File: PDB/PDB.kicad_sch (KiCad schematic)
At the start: 45 parts, among them J1 Conn_01x02, J2 Conn_01x04, Q1 S8050, Sw1 D-SWITCH_MR5-111-C5N-BB

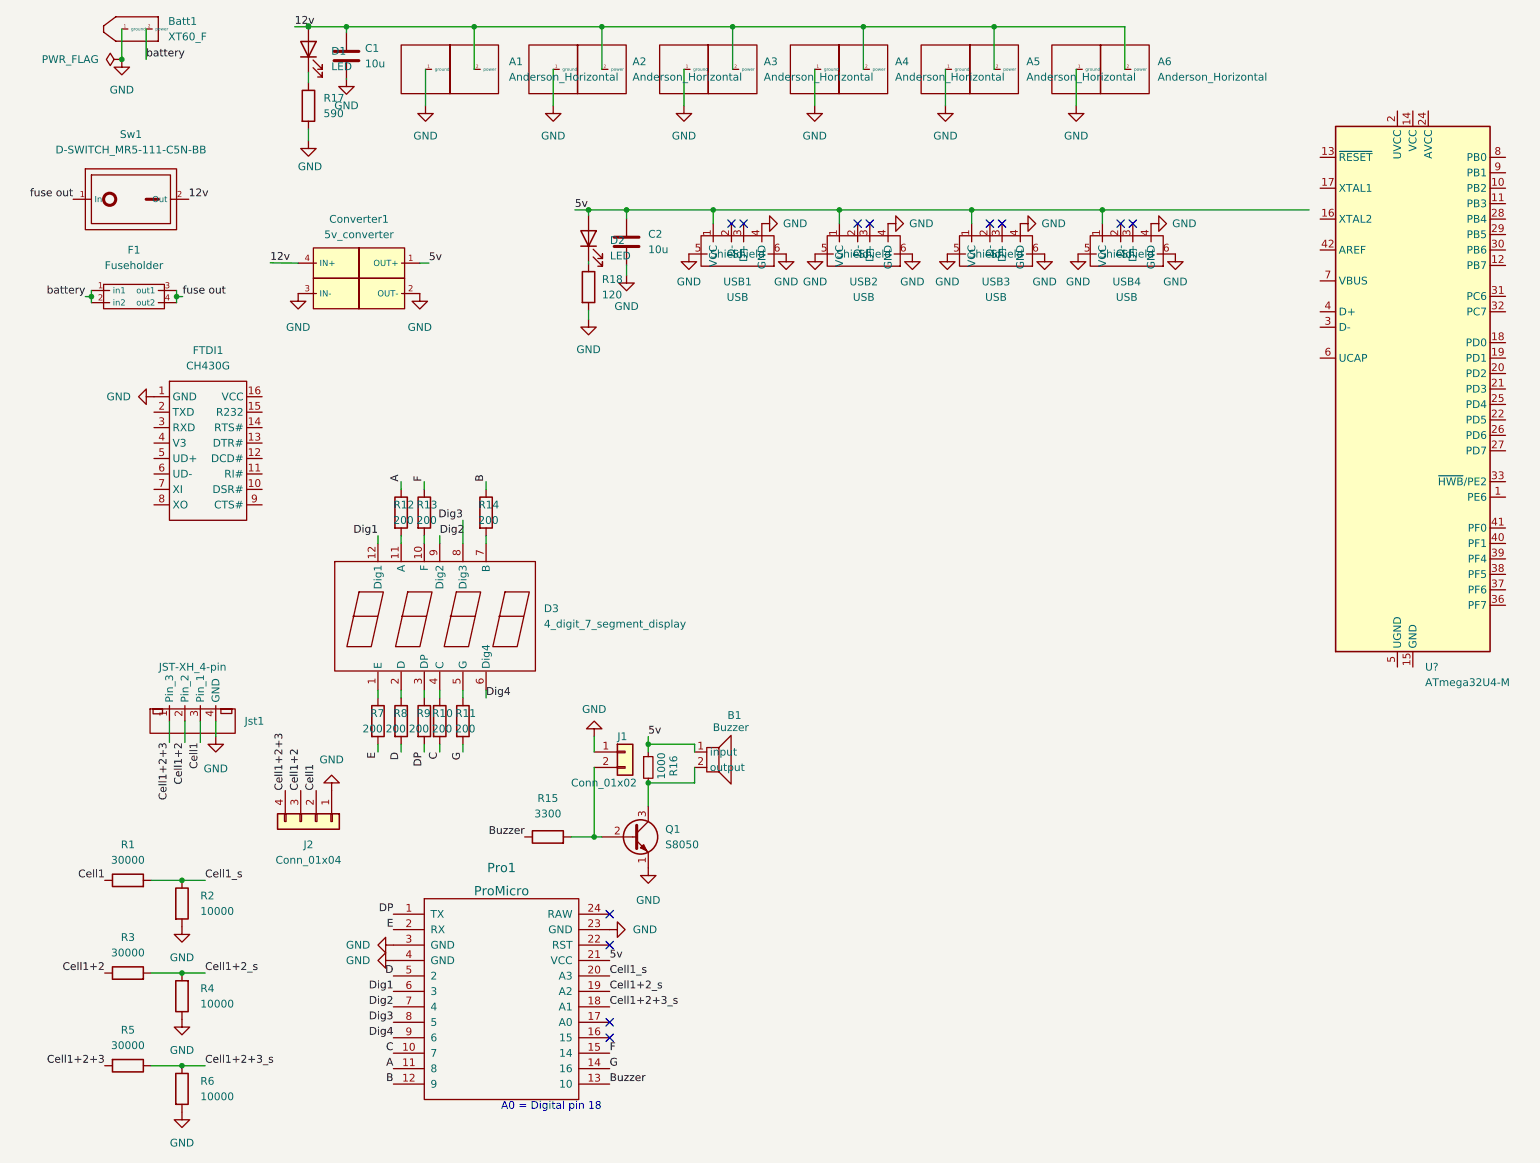
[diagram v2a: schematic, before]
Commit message: revised layout for smaller size
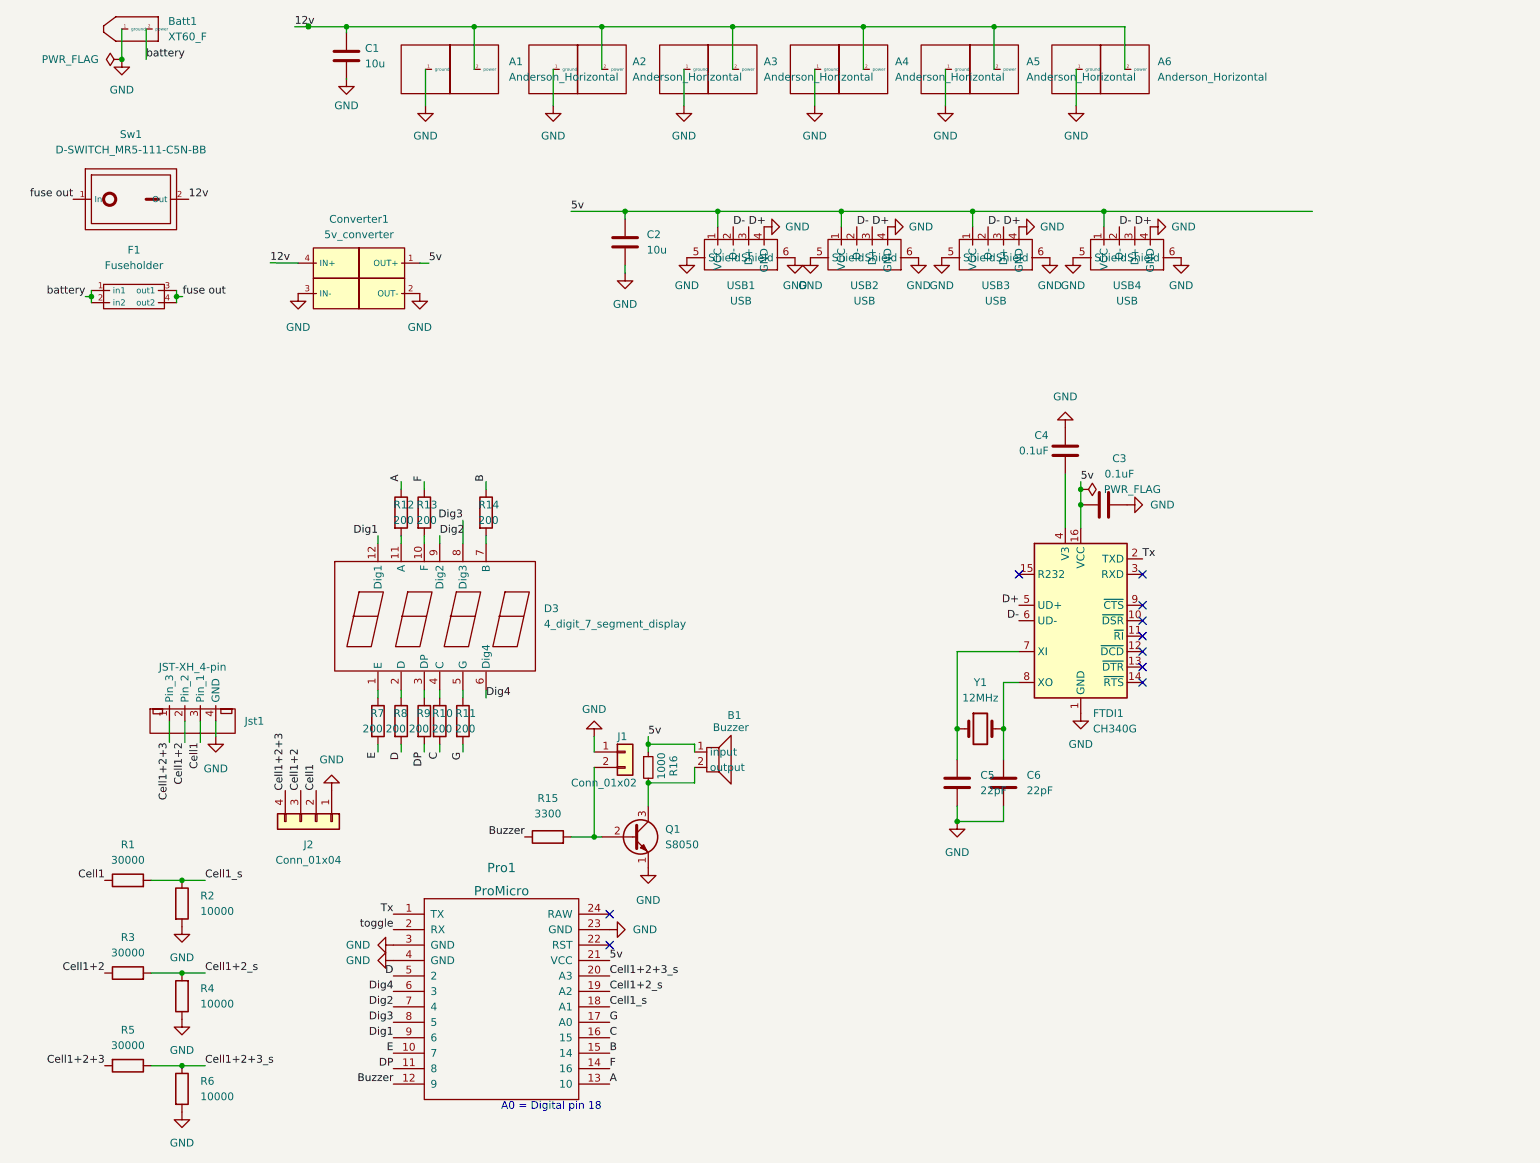
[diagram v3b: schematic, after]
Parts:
- removed D1, D2: LED, LED_SMD:LED_0603_1608Metric, symbol Device:LED
- removed FTDI1: CH430G, symbol PiE_Symbols:CH430G
- removed R17: 590, Resistor_SMD:R_1210_3225Metric, symbol Device:R
- removed R18: 120, Resistor_SMD:R_0603_1608Metric, symbol Device:R
- removed U?: ATmega32U4-M, Package_DFN_QFN:QFN-44-1EP_7x7mm_P0.5mm_EP5.2x5.2mm, symbol MCU_Microchip_ATmega:ATmega32U4-M
- added C3, C4: 0.1uF, Capacitor_SMD:C_0603_1608Metric, symbol Device:C
- added C5, C6: 22pF, Capacitor_SMD:C_0603_1608Metric, symbol Device:C
- added FTDI1: CH340G, Package_SO:SOIC-16_3.9x9.9mm_P1.27mm, symbol Interface_USB:CH340G
- added Y1: 12MHz, Crystal:Crystal_HC49-U_Vertical, symbol Device:Crystal
- C1, C2: footprint Capacitor_SMD:C_0805_2012Metric -> Capacitor_THT:CP_Radial_D5.0mm_P2.00mm
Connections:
- net 5v: now also C3.1, FTDI1.16 (VCC)
- net A: now also Pro1.13 (10); no longer Pro1.11 (8)
- net B: now also Pro1.15 (14); no longer Pro1.12 (9)
- net Buzzer: now also Pro1.12 (9); no longer Pro1.13 (10)
- net C: now also Pro1.16 (15); no longer Pro1.10 (7)
- net Cell1+2+3_s: now also Pro1.20 (A3); no longer Pro1.18 (A1)
- net Cell1_s: now also Pro1.18 (A1); no longer Pro1.20 (A3)
- net DP: now also Pro1.11 (8); no longer Pro1.1 (TX)
- net Dig1: now also Pro1.9 (6); no longer Pro1.6 (3)
- net Dig4: now also Pro1.6 (3); no longer Pro1.9 (6)
- net E: now also Pro1.10 (7); no longer Pro1.2 (RX)
- net F: now also Pro1.14 (16); no longer Pro1.15 (14)
- net G: now also Pro1.17 (A0); no longer Pro1.14 (16)
- net GND: now also C3.2, C4.2, C5.2, C6.2, FTDI1.1 (GND)
- net D-: now reaches USB3.2 (D-)
- net D-: now also USB1.2 (D-), USB2.2 (D-), USB4.2 (D-), FTDI1.6 (UD-)
- net D+: now reaches USB3.3 (D+)
- net D+: now also USB1.3 (D+), USB2.3 (D+), USB4.3 (D+), FTDI1.5 (UD+)
- new net: C5.1, FTDI1.7 (XI), Y1.1
- new net: C6.1, FTDI1.8 (XO), Y1.2
- new net: C4.1, FTDI1.4 (V3)
- new net Tx: FTDI1.2 (TXD), Pro1.1 (TX)
- new net toggle: Pro1.2 (RX)
- no-connect marks 12 -> 10
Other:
- moved on the sheet: USB1, USB2, USB3, USB4

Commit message: Finished board layout?
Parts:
- added C7: 0.1u, Capacitor_SMD:C_0603_1608Metric, symbol Device:C
- added R17, R18: 22, Resistor_SMD:R_0603_1608Metric, symbol Device:R
- added SW2: SW_SPDT, PiE_Footprints:DEALON SS-12D01-G3, symbol Switch:SW_SPDT
- added U3: PCF8574, PiE_Footprints:PCF8574T, symbol Interface_Expansion:PCF8574
- Batt1: footprint PiE_Footprints:XT60_F -> PiE_Footprints:AMASS_XT60-M_1x02_P7.20mm_Vertical
- J1: footprint Connector_PinHeader_2.54mm:PinHeader_1x02_P2.54mm_Vertical -> PiE_Footprints:PinHeader_1x02_P2.54mm_Vertical
- J2: footprint Connector_PinHeader_2.54mm:PinHeader_1x04_P2.54mm_Vertical -> PiE_Footprints:PinHeader_1x04_P2.54mm_Vertical
- Jst1: footprint PiE_Footprints:JST_XH_B4B-XH-AM_1x04_P2.50mm_Vertical -> PiE_Footprints:JST_XH_B4B-XH-A_1x04_P2.50mm_Vertical
- Y1: footprint Crystal:Crystal_HC49-U_Vertical -> PiE_Footprints:JYJE S1C12000VWFAC
- renumbered USB4 to DATA1, FTDI1 to U2
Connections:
- net 5v: now also C7.2, SW2.1 (A), U3.16 (VDD)
- net A: now also U3.7 (P3); no longer Pro1.13 (10)
- net B: now also U3.9 (P4); no longer Pro1.15 (14)
- net Buzzer: now also Pro1.13 (10); no longer Pro1.12 (9)
- net C: now also U3.11 (P6); no longer Pro1.16 (15)
- net Cell1+2+3_s: now also Pro1.18 (A1); no longer Pro1.20 (A3)
- net Cell1_s: now also Pro1.20 (A3); no longer Pro1.18 (A1)
- net D: now also U3.5 (P1); no longer Pro1.5 (2)
- net D+: now also R18.1; no longer DATA1.3 (D+), USB1.3 (D+), USB2.3 (D+), USB3.3 (D+)
- net D-: now also R17.1; no longer DATA1.2 (D-), USB1.2 (D-), USB2.2 (D-), USB3.2 (D-)
- net DP: now also U3.6 (P2); no longer Pro1.11 (8)
- net Dig1: now also Pro1.17 (A0); no longer Pro1.9 (6)
- net Dig2: now also Pro1.16 (15); no longer Pro1.7 (4)
- net Dig3: now also Pro1.15 (14); no longer Pro1.8 (5)
- net Dig4: now also Pro1.12 (9); no longer Pro1.6 (3)
- net E: now also U3.4 (P0); no longer Pro1.10 (7)
- net F: now also U3.10 (P5); no longer Pro1.14 (16)
- net G: now also U3.12 (P7); no longer Pro1.17 (A0)
- net GND: now also C7.1, SW2.3 (C), U3.1 (A0), U3.2 (A1), U3.3 (A2), U3.8 (VSS)
- net toggle: now also Pro1.14 (16), SW2.2 (B); no longer Pro1.2 (RX)
- net Rx: now reaches U2.3 (RXD)
- net Rx: now also Pro1.2 (RX)
- new net: DATA1.3 (D+), R18.2
- new net: DATA1.2 (D-), R17.2
- new net SCL: Pro1.6 (3), U3.14 (SCL)
- new net SDA: Pro1.5 (2), U3.15 (SDA)
- no-connect marks 10 -> 16
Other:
- moved on the sheet: B1, C2, C3, C4, C5, C6, Converter1, D3, DATA1, J1, J2, Q1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

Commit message: ordered this ****
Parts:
- added R19, R20: 4700, Resistor_SMD:R_0603_1608Metric, symbol Device:R
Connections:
- net 5v: now also R19.1, R20.1
- net SCL: now also R19.2
- net SDA: now also R20.2
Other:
- moved on the sheet: C7
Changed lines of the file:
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@@
   (junction (at 38 61) (diameter 0) (color 0 0 0 0)
   )
+  (junction (at 205.74 101.6) (diameter 0) (color 0 0 0 0)
+  )
   (junction (at 238.76 46.99) (diameter 0) (color 0 0 0 0)
   )
   (junction (at 38.89 157) (diameter 0) (color 0 0 0 0)
   )
+  (junction (at 220.98 88.9) (diameter 0) (color 0 0 0 0)
+  )
   (junction (at 125.73 40.64) (diameter 0) (color 0 0 0 0)
   )
@@
   (junction (at 92.71 97.79) (diameter 0) (color 0 0 0 0)
   )
-  (junction (at 220.98 88.9) (diameter 0) (color 0 0 0 0)
-  )
   (junction (at 92.71 100.33) (diameter 0) (color 0 0 0 0)
   )
   (junction (at 59.69 16.63) (diameter 0) (color 0 0 0 0)
   )
+  (junction (at 205.74 88.9) (diameter 0) (color 0 0 0 0)
+  )
   (junction (at 38.89 187.48) (diameter 0) (color 0 0 0 0)
+  )
+  (junction (at 201.93 99.06) (diameter 0) (color 0 0 0 0)
   )
   (junction (at 29 22) (diameter 0) (color 0 0 0 0)
@@
     (stroke (width 0) (type default) (color 0 0 0 0))
   )
+  (wire (pts (xy 200.66 101.6) (xy 205.74 101.6))
+    (stroke (width 0) (type default) (color 0 0 0 0))
+  )
   (wire (pts (xy 39.37 130.81) (xy 39.37 134.31))
     (stroke (width 0) (type default) (color 0 0 0 0))
@@
     (stroke (width 0) (type default) (color 0 0 0 0))
   )
+  (wire (pts (xy 205.74 88.9) (xy 220.98 88.9))
+    (stroke (width 0) (type default) (color 0 0 0 0))
+  )
   (wire (pts (xy 38 61) (xy 38 62))
     (stroke (width 0) (type default) (color 0 0 0 0))
@@
     (stroke (width 0) (type default) (color 0 0 0 0))
   )
+  (wire (pts (xy 220.98 88.9) (xy 220.98 91.44))
+    (stroke (width 0) (type default) (color 0 0 0 0))
+  )
   (wire (pts (xy 72.39 124.46) (xy 72.39 132.08))
     (stroke (width 0) (type default) (color 0 0 0 0))
@@
     (stroke (width 0) (type default) (color 0 0 0 0))
   )
+  (wire (pts (xy 201.93 99.06) (xy 208.28 99.06))
+    (stroke (width 0) (type default) (color 0 0 0 0))
+  )
   (wire (pts (xy 44.45 130.81) (xy 44.45 133.35))
     (stroke (width 0) (type default) (color 0 0 0 0))
@@
     (stroke (width 0) (type default) (color 0 0 0 0))
   )
+  (wire (pts (xy 205.74 88.9) (xy 205.74 93.98))
+    (stroke (width 0) (type default) (color 0 0 0 0))
+  )
   (wire (pts (xy 129.44 16.63) (xy 129.44 23.63))
     (stroke (width 0) (type default) (color 0 0 0 0))
@@
     (stroke (width 0) (type default) (color 0 0 0 0))
   )
+  (wire (pts (xy 201.93 91.44) (xy 201.93 88.9))
+    (stroke (width 0) (type default) (color 0 0 0 0))
+  )
+  (wire (pts (xy 205.74 101.6) (xy 208.28 101.6))
+    (stroke (width 0) (type default) (color 0 0 0 0))
+  )
   (wire (pts (xy 172.44 16.63) (xy 172.44 23.63))
     (stroke (width 0) (type default) (color 0 0 0 0))
@@
     (stroke (width 0) (type default) (color 0 0 0 0))
   )
-  (wire (pts (xy 220.98 88.9) (xy 220.98 91.44))
-    (stroke (width 0) (type default) (color 0 0 0 0))
-  )
   (wire (pts (xy 90.17 40.64) (xy 90.17 41.91))
     (stroke (width 0) (type default) (color 0 0 0 0))
@@
     (stroke (width 0) (type default) (color 0 0 0 0))
   )
+  (wire (pts (xy 200.66 99.06) (xy 201.93 99.06))
+    (stroke (width 0) (type default) (color 0 0 0 0))
+  )
   (wire (pts (xy 208.28 111.76) (xy 205.74 111.76))
     (stroke (width 0) (type default) (color 0 0 0 0))
@@
     (stroke (width 0) (type default) (color 0 0 0 0))
   )
+  (wire (pts (xy 201.93 88.9) (xy 205.74 88.9))
+    (stroke (width 0) (type default) (color 0 0 0 0))
+  )
   (wire (pts (xy 24 60) (xy 24 61))
     (stroke (width 0) (type default) (color 0 0 0 0))
@@
     (stroke (width 0) (type default) (color 0 0 0 0))
   )
+  (wire (pts (xy 220.98 80.01) (xy 220.98 88.9))
+    (stroke (width 0) (type default) (color 0 0 0 0))
+  )
   (wire (pts (xy 172.44 16.63) (xy 193.94 16.63))
     (stroke (width 0) (type default) (color 0 0 0 0))
@@
     (stroke (width 0) (type default) (color 0 0 0 0))
   )
-  (wire (pts (xy 220.98 85.09) (xy 220.98 88.9))
-    (stroke (width 0) (type default) (color 0 0 0 0))
-  )
   (wire (pts (xy 170.18 157.48) (xy 170.18 158.75))
     (stroke (width 0) (type default) (color 0 0 0 0))
@@
     (effects (font (size 1.27 1.27)) (justify left bottom))
   )
-  (label "SCL" (at 208.28 99.06 180)
+  (label "SCL" (at 200.66 99.06 180)
     (effects (font (size 1.27 1.27)) (justify right bottom))
   )
@@
     (effects (font (size 1.27 1.27)) (justify left bottom))
   )
-  (label "5v" (at 220.98 85.09 180)
-    (effects (font (size 1.27 1.27)) (justify right bottom))
+  (label "5v" (at 220.98 81.28 0)
+    (effects (font (size 1.27 1.27)) (justify left bottom))
   )
   (label "battery" (at 33 22 0)
@@
     (effects (font (size 1.27 1.27)) (justify right bottom))
   )
-  (label "SDA" (at 208.28 101.6 180)
+  (label "SDA" (at 200.66 101.6 180)
     (effects (font (size 1.27 1.27)) (justify right bottom))
   )
@@
     (pin "2")
   )
+  (symbol (lib_id "Device:R") (at 205.74 97.79 0) (unit 1)
+    (in_bom yes) (on_board yes)
+    (property "Reference" "R20" (id 0) (at 207.01 93.98 0)
+      (effects (font (size 1.27 1.27)) (justify left))
+    )
+    (property "Value" "4700" (id 1) (at 207.01 96.52 0)
+      (effects (font (size 1.27 1.27)) (justify left))
+    )
+    (property "Footprint" "Resistor_SMD:R_0603_1608Metric" (id 2) (at 203.962 97.79 90)
+      (effects (font (size 1.27 1.27)) hide)
+    )
+    (property "Datasheet" "~" (id 3) (at 205.74 97.79 0)
+      (effects (font (size 1.27 1.27)) hide)
+    )
+    (pin "1")
+    (pin "2")
+  )
   (symbol (lib_id "PiE_Symbols:Anderson_Horizontal") (at 125.44 19.63 0) (unit 1)
     (in_bom yes) (on_board yes) (fields_autoplaced)
@@
     (pin "1")
   )
-  (symbol (lib_id "Device:C") (at 217.17 88.9 90) (unit 1)
+  (symbol (lib_id "Device:C") (at 217.17 80.01 90) (unit 1)
     (in_bom yes) (on_board yes)
-    (property "Reference" "C7" (id 0) (at 214.63 81.28 90))
-    (property "Value" "0.1u" (id 1) (at 214.63 83.82 90))
-    (property "Footprint" "Capacitor_SMD:C_0603_1608Metric" (id 2) (at 220.98 87.9348 0)
-      (effects (font (size 1.27 1.27)) hide)
-    )
-    (property "Datasheet" "~" (id 3) (at 217.17 88.9 0)
+    (property "Reference" "C7" (id 0) (at 214.63 72.39 90))
+    (property "Value" "0.1u" (id 1) (at 214.63 74.93 90))
+    (property "Footprint" "Capacitor_SMD:C_0603_1608Metric" (id 2) (at 220.98 79.0448 0)
+      (effects (font (size 1.27 1.27)) hide)
+    )
+    (property "Datasheet" "~" (id 3) (at 217.17 80.01 0)
       (effects (font (size 1.27 1.27)) hide)
     )
@@
     (pin "2")
   )
+  (symbol (lib_id "Device:R") (at 201.93 95.25 0) (unit 1)
+    (in_bom yes) (on_board yes)
+    (property "Reference" "R19" (id 0) (at 198.12 92.71 0)
+      (effects (font (size 1.27 1.27)) (justify left))
+    )
+    (property "Value" "4700" (id 1) (at 199.39 95.25 0)
+      (effects (font (size 1.27 1.27)) (justify left))
+    )
+    (property "Footprint" "Resistor_SMD:R_0603_1608Metric" (id 2) (at 200.152 95.25 90)
+      (effects (font (size 1.27 1.27)) hide)
+    )
+    (property "Datasheet" "~" (id 3) (at 201.93 95.25 0)
+      (effects (font (size 1.27 1.27)) hide)
+    )
+    (pin "1")
+    (pin "2")
+  )
   (symbol (lib_id "power:GND") (at 72.39 143.51 0) (unit 1)
     (in_bom yes) (on_board yes) (fields_autoplaced)
@@
     (pin "1")
   )
-  (symbol (lib_id "power:GND") (at 213.36 88.9 270) (unit 1)
-    (in_bom yes) (on_board yes) (fields_autoplaced)
-    (property "Reference" "#PWR0141" (id 0) (at 207.01 88.9 0)
-      (effects (font (size 1.27 1.27)) hide)
-    )
-    (property "Value" "GND" (id 1) (at 209.55 88.8999 90)
+  (symbol (lib_id "power:GND") (at 213.36 80.01 270) (unit 1)
+    (in_bom yes) (on_board yes) (fields_autoplaced)
+    (property "Reference" "#PWR0141" (id 0) (at 207.01 80.01 0)
+      (effects (font (size 1.27 1.27)) hide)
+    )
+    (property "Value" "GND" (id 1) (at 209.55 80.0099 90)
       (effects (font (size 1.27 1.27)) (justify right))
     )
-    (property "Footprint" "" (id 2) (at 213.36 88.9 0)
-      (effects (font (size 1.27 1.27)) hide)
-    )
-    (property "Datasheet" "" (id 3) (at 213.36 88.9 0)
+    (property "Footprint" "" (id 2) (at 213.36 80.01 0)
+      (effects (font (size 1.27 1.27)) hide)
+    )
+    (property "Datasheet" "" (id 3) (at 213.36 80.01 0)
       (effects (font (size 1.27 1.27)) hide)
     )
@@
       (reference "R18") (unit 1) (value "22") (footprint "Resistor_SMD:R_0603_1608Metric")
     )
+    (path "/b1354165-9d38-48cc-915e-604c4ea36f99"
+      (reference "R19") (unit 1) (value "4700") (footprint "Resistor_SMD:R_0603_1608Metric")
+    )
+    (path "/6bf9f400-2353-4b42-a607-dbe649b6781c"
+      (reference "R20") (unit 1) (value "4700") (footprint "Resistor_SMD:R_0603_1608Metric")
+    )
     (path "/7bb25490-f7a1-43ab-a25a-ef27108cc305"

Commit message: fixed PDB layout
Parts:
- removed A6: Anderson_Horizontal, PiE_Footprints:anderson_horizontal, symbol PiE_Symbols:Anderson_Horizontal
- removed Q1: S8050, PiE_Footprints:s8050 SMD, symbol Transistor_BJT:S8050
- added Q1: s8050_JSMSEMI, PiE_Footprints:s8050 JSMSEMI, symbol PiE_Symbols:s8050_JSMSEMI
- U2: footprint Package_SO:SOIC-16_3.9x9.9mm_P1.27mm -> PiE_Footprints:CH340g
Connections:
- net B: now also U3.11 (P6); no longer U3.9 (P4)
- net C: now also U3.10 (P5); no longer U3.11 (P6)
- net F: now also U3.12 (P7); no longer U3.10 (P5)
- net G: now also U3.9 (P4); no longer U3.12 (P7)
- net GND: now also Q1.2 (E)
- net Rx: now also U2.2 (TXD); no longer U2.3 (RXD)
- net Tx: now also U2.3 (RXD); no longer U2.2 (TXD)
- net collector: now reaches B1.2 (output), R16.2
- net collector: now also Q1.3 (C)
- net base: now reaches J1.2 (Pin_2), R15.2
- net base: now also Q1.1 (B)
- no-connect marks 16 -> 21
